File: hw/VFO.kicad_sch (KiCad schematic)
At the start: 8 parts, among them U7703 74HC74, U7704 74HC74, Y7701 25MHz FA-238 25.0000MB-K, Y7702 Si5351A-B-GM

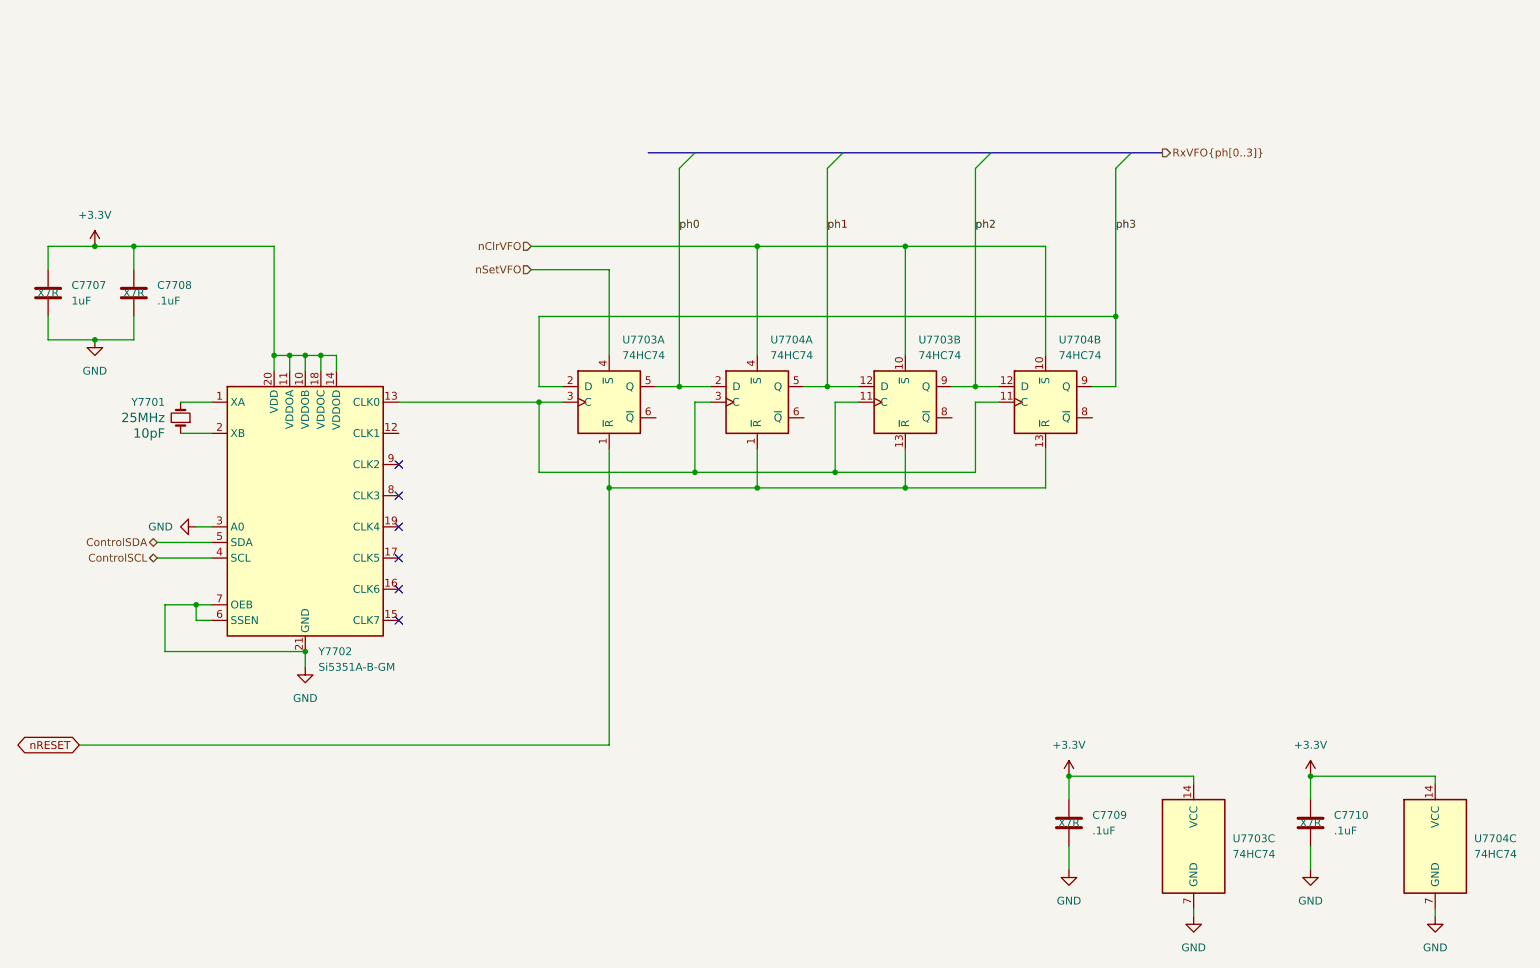
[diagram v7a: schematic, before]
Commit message: Getting closer to having all (ten) BPFs designed. Maybe I can try some layout next.
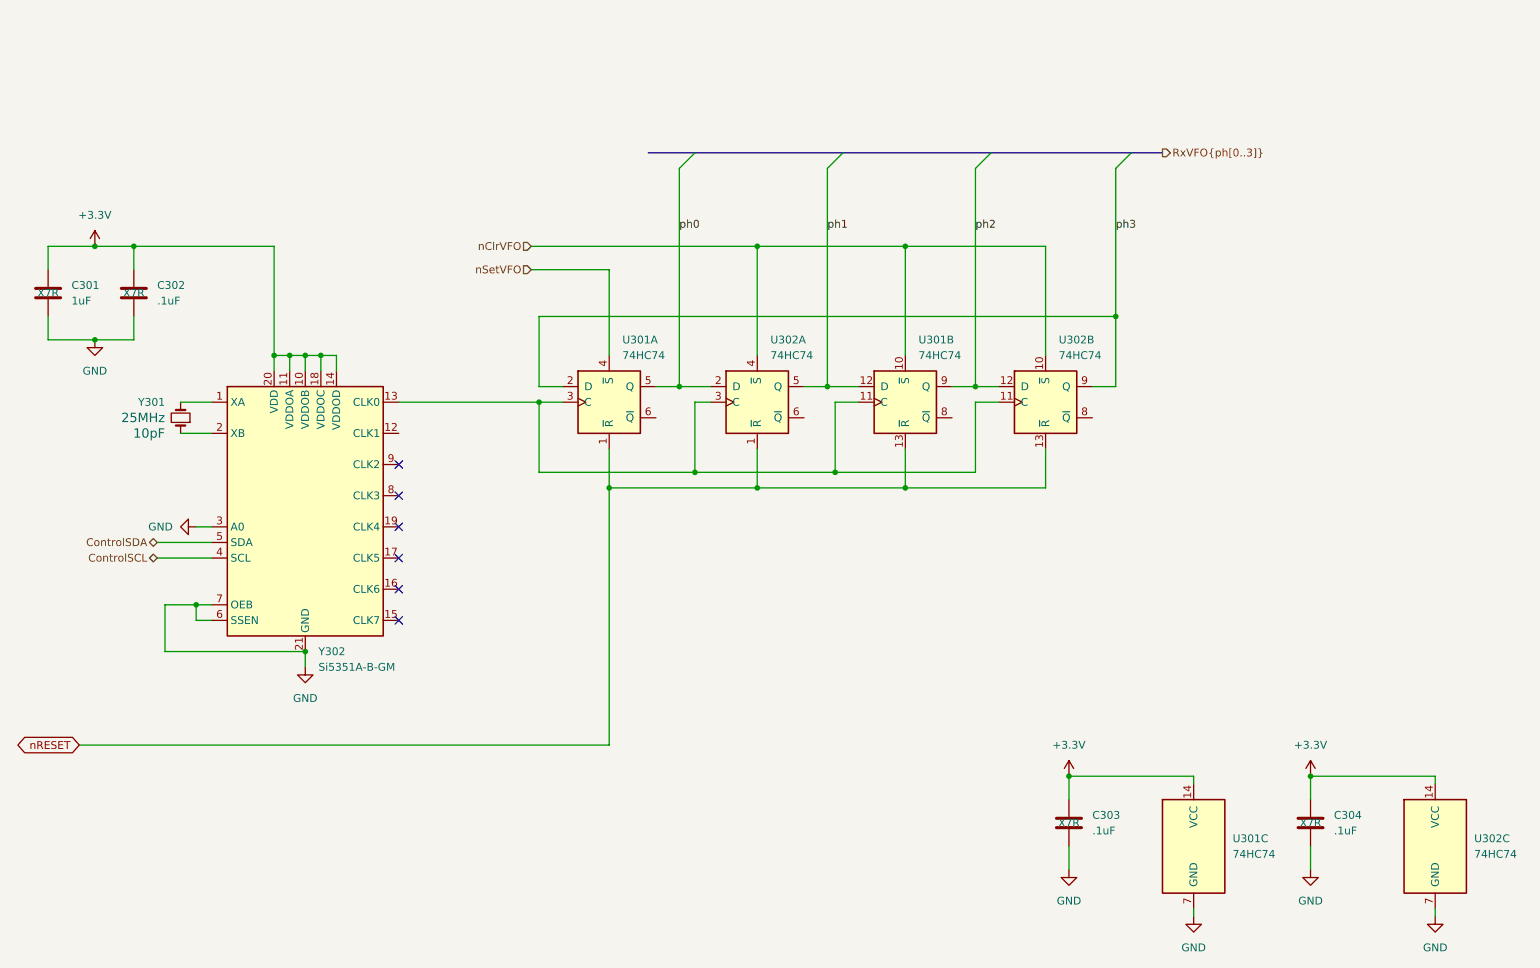
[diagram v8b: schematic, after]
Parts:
- renumbered C7707 to C301, C7708 to C302, C7709 to C303, C7710 to C304, U7703 to U301, U7704 to U302, Y7701 to Y301, Y7702 to Y302
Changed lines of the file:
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@@
 		(dnp no)
 		(fields_autoplaced yes)
-		(property "Reference" "C7709"
+		(property "Reference" "C303"
 			(at 195.58 146.0499 0)
 			(effects
@@
 			(project "USB-SSB-txcvr"
 				(path "/8ae46c04-d01a-4756-8774-512b694bfaff/dab9d1f1-a255-4db5-bc55-08fa1f9f2738"
-					(reference "C7709")
+					(reference "C303")
 					(unit 1)
 				)
@@
 		(dnp no)
 		(fields_autoplaced yes)
-		(property "Reference" "C7708"
+		(property "Reference" "C302"
 			(at 43.18 59.6899 0)
 			(effects
@@
 			(project "USB-SSB-txcvr"
 				(path "/8ae46c04-d01a-4756-8774-512b694bfaff/dab9d1f1-a255-4db5-bc55-08fa1f9f2738"
-					(reference "C7708")
+					(reference "C302")
 					(unit 1)
 				)
@@
 		(dnp no)
 		(fields_autoplaced yes)
-		(property "Reference" "#PWR07719"
+		(property "Reference" "#PWR0306"
 			(at 191.77 161.29 0)
 			(effects
@@
 			(project "USB-SSB-txcvr"
 				(path "/8ae46c04-d01a-4756-8774-512b694bfaff/dab9d1f1-a255-4db5-bc55-08fa1f9f2738"
-					(reference "#PWR07719")
+					(reference "#PWR0306")
 					(unit 1)
 				)
@@
 		(on_board yes)
 		(dnp no)
-		(property "Reference" "#PWR07721"
+		(property "Reference" "#PWR0308"
 			(at 231.14 143.51 0)
 			(effects
@@
 			(project "USB-SSB-txcvr"
 				(path "/8ae46c04-d01a-4756-8774-512b694bfaff/dab9d1f1-a255-4db5-bc55-08fa1f9f2738"
-					(reference "#PWR07721")
+					(reference "#PWR0308")
 					(unit 1)
 				)
@@
 		(dnp no)
 		(fields_autoplaced yes)
-		(property "Reference" "Y7702"
+		(property "Reference" "Y302"
 			(at 69.4533 119.38 0)
 			(effects
@@
 			(project ""
 				(path "/8ae46c04-d01a-4756-8774-512b694bfaff/dab9d1f1-a255-4db5-bc55-08fa1f9f2738"
-					(reference "Y7702")
+					(reference "Y302")
 					(unit 1)
 				)
@@
 		(dnp no)
 		(fields_autoplaced yes)
-		(property "Reference" "#PWR07716"
+		(property "Reference" "#PWR0303"
 			(at 43.18 99.06 0)
 			(effects
@@
 			(project ""
 				(path "/8ae46c04-d01a-4756-8774-512b694bfaff/dab9d1f1-a255-4db5-bc55-08fa1f9f2738"
-					(reference "#PWR07716")
+					(reference "#PWR0303")
 					(unit 1)
 				)
@@
 		(dnp no)
 		(fields_autoplaced yes)
-		(property "Reference" "C7707"
+		(property "Reference" "C301"
 			(at 29.21 59.6899 0)
 			(effects
@@
 			(project ""
 				(path "/8ae46c04-d01a-4756-8774-512b694bfaff/dab9d1f1-a255-4db5-bc55-08fa1f9f2738"
-					(reference "C7707")
+					(reference "C301")
 					(unit 1)
 				)
@@
 		(on_board yes)
 		(dnp no)
-		(property "Reference" "#PWR07718"
+		(property "Reference" "#PWR0305"
 			(at 191.77 143.51 0)
 			(effects
@@
 			(project "USB-SSB-txcvr"
 				(path "/8ae46c04-d01a-4756-8774-512b694bfaff/dab9d1f1-a255-4db5-bc55-08fa1f9f2738"
-					(reference "#PWR07718")
+					(reference "#PWR0305")
 					(unit 1)
 				)
@@
 		(dnp no)
 		(fields_autoplaced yes)
-		(property "Reference" "C7710"
+		(property "Reference" "C304"
 			(at 234.95 146.0499 0)
 			(effects
@@
 			(project "USB-SSB-txcvr"
 				(path "/8ae46c04-d01a-4756-8774-512b694bfaff/dab9d1f1-a255-4db5-bc55-08fa1f9f2738"
-					(reference "C7710")
+					(reference "C304")
 					(unit 1)
 				)
@@
 		(dnp no)
 		(fields_autoplaced yes)
-		(property "Reference" "U7703"
+		(property "Reference" "U301"
 			(at 218.44 149.8599 0)
 			(effects
@@
 			(project ""
 				(path "/8ae46c04-d01a-4756-8774-512b694bfaff/dab9d1f1-a255-4db5-bc55-08fa1f9f2738"
-					(reference "U7703")
+					(reference "U301")
 					(unit 3)
 				)
@@
 		(dnp no)
 		(fields_autoplaced yes)
-		(property "Reference" "U7704"
+		(property "Reference" "U302"
 			(at 190.1033 68.58 0)
 			(effects
@@
 			(project "USB-SSB-txcvr"
 				(path "/8ae46c04-d01a-4756-8774-512b694bfaff/dab9d1f1-a255-4db5-bc55-08fa1f9f2738"
-					(reference "U7704")
+					(reference "U302")
 					(unit 2)
 				)
@@
 		(dnp no)
 		(fields_autoplaced yes)
-		(property "Reference" "#PWR07723"
+		(property "Reference" "#PWR0310"
 			(at 251.46 168.91 0)
 			(effects
@@
 			(project "USB-SSB-txcvr"
 				(path "/8ae46c04-d01a-4756-8774-512b694bfaff/dab9d1f1-a255-4db5-bc55-08fa1f9f2738"
-					(reference "#PWR07723")
+					(reference "#PWR0310")
 					(unit 1)
 				)
@@
 		(on_board yes)
 		(dnp no)
-		(property "Reference" "Y7701"
+		(property "Reference" "Y301"
 			(at 44.45 78.7399 90)
 			(effects
@@
 			(project ""
 				(path "/8ae46c04-d01a-4756-8774-512b694bfaff/dab9d1f1-a255-4db5-bc55-08fa1f9f2738"
-					(reference "Y7701")
+					(reference "Y301")
 					(unit 1)
 				)
@@
 		(dnp no)
 		(fields_autoplaced yes)
-		(property "Reference" "#PWR07717"
+		(property "Reference" "#PWR0304"
 			(at 67.31 128.27 0)
 			(effects
@@
 			(project "USB-SSB-txcvr"
 				(path "/8ae46c04-d01a-4756-8774-512b694bfaff/dab9d1f1-a255-4db5-bc55-08fa1f9f2738"
-					(reference "#PWR07717")
+					(reference "#PWR0304")
 					(unit 1)
 				)
@@
 		(dnp no)
 		(fields_autoplaced yes)
-		(property "Reference" "U7703"
+		(property "Reference" "U301"
 			(at 118.9833 68.58 0)
 			(effects
@@
 			(project ""
 				(path "/8ae46c04-d01a-4756-8774-512b694bfaff/dab9d1f1-a255-4db5-bc55-08fa1f9f2738"
-					(reference "U7703")
+					(reference "U301")
 					(unit 1)
 				)
@@
 		(dnp no)
 		(fields_autoplaced yes)
-		(property "Reference" "#PWR07720"
+		(property "Reference" "#PWR0307"
 			(at 212.09 168.91 0)
 			(effects
@@
 			(project "USB-SSB-txcvr"
 				(path "/8ae46c04-d01a-4756-8774-512b694bfaff/dab9d1f1-a255-4db5-bc55-08fa1f9f2738"
-					(reference "#PWR07720")
+					(reference "#PWR0307")
 					(unit 1)
 				)
@@
 		(dnp no)
 		(fields_autoplaced yes)
-		(property "Reference" "#PWR07722"
+		(property "Reference" "#PWR0309"
 			(at 231.14 161.29 0)
 			(effects
@@
 			(project "USB-SSB-txcvr"
 				(path "/8ae46c04-d01a-4756-8774-512b694bfaff/dab9d1f1-a255-4db5-bc55-08fa1f9f2738"
-					(reference "#PWR07722")
+					(reference "#PWR0309")
 					(unit 1)
 				)
@@
 		(dnp no)
 		(fields_autoplaced yes)
-		(property "Reference" "#PWR07715"
+		(property "Reference" "#PWR0302"
 			(at 33.02 74.93 0)
 			(effects
@@
 			(project "USB-SSB-txcvr"
 				(path "/8ae46c04-d01a-4756-8774-512b694bfaff/dab9d1f1-a255-4db5-bc55-08fa1f9f2738"
-					(reference "#PWR07715")
+					(reference "#PWR0302")
 					(unit 1)
 				)
@@
 		(dnp no)
 		(fields_autoplaced yes)
-		(property "Reference" "U7703"
+		(property "Reference" "U301"
 			(at 167.2433 68.58 0)
 			(effects
@@
 			(project ""
 				(path "/8ae46c04-d01a-4756-8774-512b694bfaff/dab9d1f1-a255-4db5-bc55-08fa1f9f2738"
-					(reference "U7703")
+					(reference "U301")
 					(unit 2)
 				)
@@
 		(dnp no)
 		(fields_autoplaced yes)
-		(property "Reference" "#PWR07714"
+		(property "Reference" "#PWR0301"
 			(at 33.02 57.15 0)
 			(effects
@@
 			(project "USB-SSB-txcvr"
 				(path "/8ae46c04-d01a-4756-8774-512b694bfaff/dab9d1f1-a255-4db5-bc55-08fa1f9f2738"
-					(reference "#PWR07714")
+					(reference "#PWR0301")
 					(unit 1)
 				)
@@
 		(dnp no)
 		(fields_autoplaced yes)
-		(property "Reference" "U7704"
+		(property "Reference" "U302"
 			(at 257.81 149.8599 0)
 			(effects
@@
 			(project "USB-SSB-txcvr"
 				(path "/8ae46c04-d01a-4756-8774-512b694bfaff/dab9d1f1-a255-4db5-bc55-08fa1f9f2738"
-					(reference "U7704")
+					(reference "U302")
 					(unit 3)
 				)
@@
 		(dnp no)
 		(fields_autoplaced yes)
-		(property "Reference" "U7704"
+		(property "Reference" "U302"
 			(at 143.1133 68.58 0)
 			(effects
@@
 			(project "USB-SSB-txcvr"
 				(path "/8ae46c04-d01a-4756-8774-512b694bfaff/dab9d1f1-a255-4db5-bc55-08fa1f9f2738"
-					(reference "U7704")
-					(unit 1)
-				)
+					(reference "U302")
+					(unit 1)
+				)
